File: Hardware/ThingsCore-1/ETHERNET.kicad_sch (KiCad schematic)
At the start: 1 part, among them U6 LAN8742A

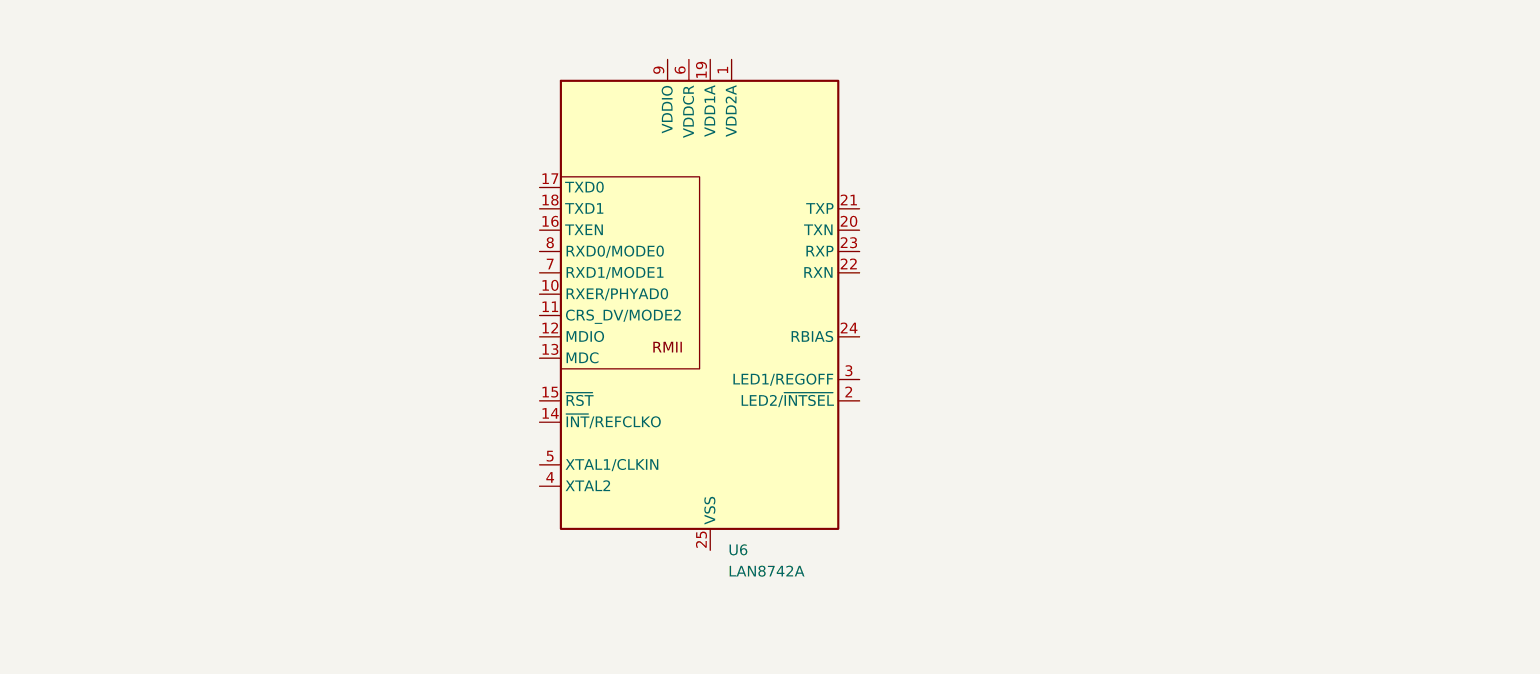
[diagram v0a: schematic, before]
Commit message: ddr3 fanout done
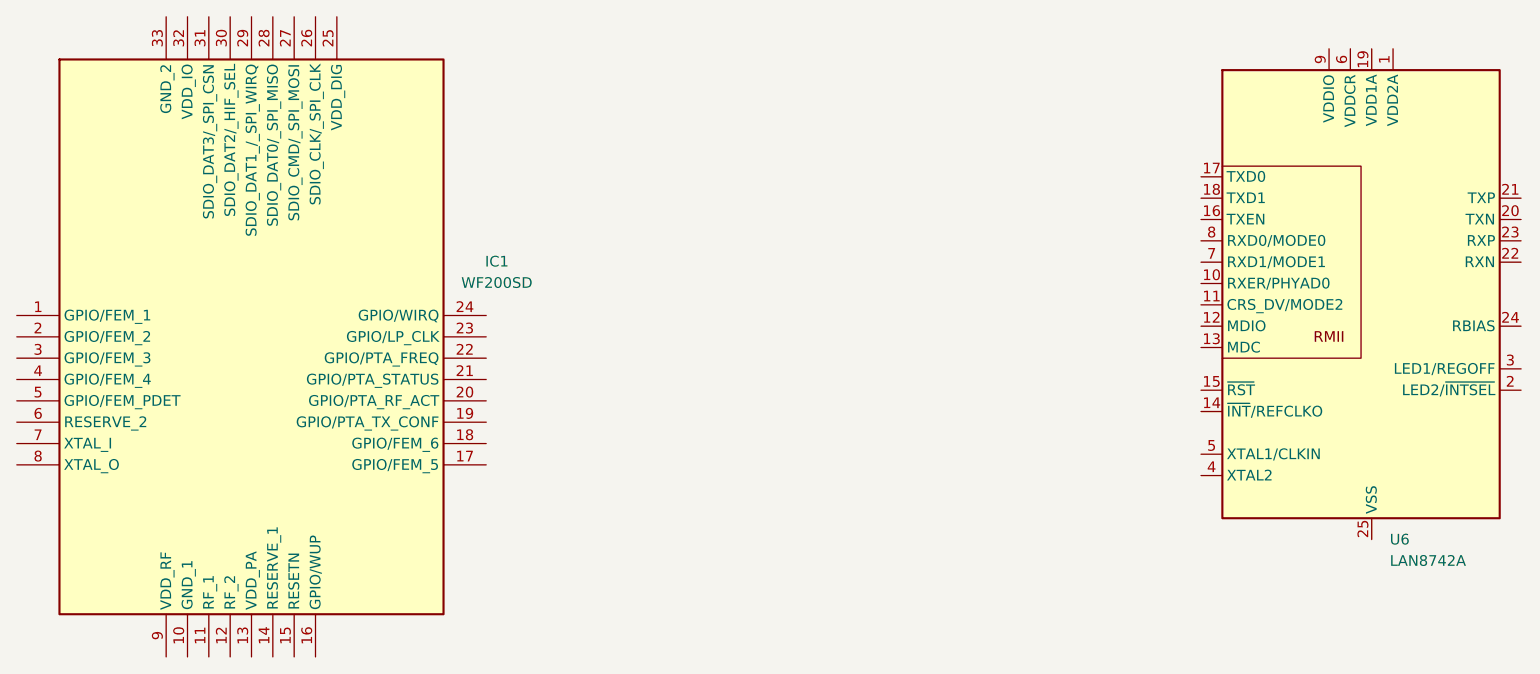
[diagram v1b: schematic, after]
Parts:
- added IC1: WF200SD, QFN40P400X400X90-33N-D, symbol ThingsCore-1:WF200SD
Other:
- moved on the sheet: U6
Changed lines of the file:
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@@
 	(symbol
 		(lib_id "Interface_Ethernet:LAN8742A")
-		(at 151.13 92.71 0)
+		(at 229.87 91.44 0)
 		(unit 1)
 		(exclude_from_sim no)
@@
 		(fields_autoplaced yes)
 		(property "Reference" "U6"
-			(at 153.2733 120.65 0)
+			(at 232.0133 119.38 0)
 			(effects
 				(font
@@
 		)
 		(property "Value" "LAN8742A"
-			(at 153.2733 123.19 0)
+			(at 232.0133 121.92 0)
 			(effects
 				(font
@@
 		)
 		(property "Footprint" "Package_DFN_QFN:VQFN-24-1EP_4x4mm_P0.5mm_EP2.45x2.45mm"
-			(at 152.4 119.38 0)
+			(at 231.14 118.11 0)
 			(effects
 				(font
@@
 		)
 		(property "Datasheet" "http://ww1.microchip.com/downloads/en/DeviceDoc/8742a.pdf"
-			(at 151.13 132.08 0)
+			(at 229.87 130.81 0)
 			(effects
 				(font
@@
 		)
 		(property "Description" "LAN8720 Ethernet PHY with RMII interface, QFN-24"
-			(at 151.13 92.71 0)
+			(at 229.87 91.44 0)
 			(effects
 				(font
@@
 					(unit 1)
 				)
+			)
+		)
+	)
+	(symbol
+		(lib_id "ThingsCore-1:WF200SD")
+		(at 68.58 92.71 0)
+		(unit 1)
+		(exclude_from_sim no)
+		(in_bom yes)
+		(on_board yes)
+		(dnp no)
+		(fields_autoplaced yes)
+		(property "Reference" "IC1"
+			(at 125.73 86.2898 0)
+			(effects
+				(font
+					(size 1.27 1.27)
+				)
+			)
+		)
+		(property "Value" "WF200SD"
+			(at 125.73 88.8298 0)
+			(effects
+				(font
+					(size 1.27 1.27)
+				)
+			)
+		)
+		(property "Footprint" "QFN40P400X400X90-33N-D"
+			(at 120.65 159.69 0)
+			(effects
+				(font
+					(size 1.27 1.27)
+				)
+				(justify left top)
+				(hide yes)
+			)
+		)
+		(property "Datasheet" "https://www.silabs.com/documents/public/data-sheets/wf200-datasheet.pdf"
+			(at 120.65 259.69 0)
+			(effects
+				(font
+					(size 1.27 1.27)
+				)
+				(justify left top)
+				(hide yes)
+			)
+		)
+		(property "Description" "WF200 802.11bgn NCP, Secure link interface, 4x4 QFN32"
+			(at 68.58 92.71 0)
+			(effects
+				(font
+					(size 1.27 1.27)
+				)
+				(hide yes)
+			)
+		)
+		(property "Height" "0.9"
+			(at 120.65 459.69 0)
+			(effects
+				(font
+					(size 1.27 1.27)
+				)
+				(justify left top)
+				(hide yes)
+			)
+		)
+		(property "Mouser Part Number" "634-WF200SD"
+			(at 120.65 559.69 0)
+			(effects
+				(font
+					(size 1.27 1.27)
+				)
+				(justify left top)
+				(hide yes)
+			)
+		)
+		(property "Mouser Price/Stock" "https://www.mouser.co.uk/ProductDetail/Silicon-Labs/WF200SD?qs=vEM7xhTegWgRA5s9PPW5sw%3D%3D"
+			(at 120.65 659.69 0)
+			(effects
+				(font
+					(size 1.27 1.27)
+				)
+				(justify left top)
+				(hide yes)
+			)
+		)
+		(property "Manufacturer_Name" "Silicon Labs"
+			(at 120.65 759.69 0)
+			(effects
+				(font
+					(size 1.27 1.27)
+				)
+				(justify left top)
+				(hide yes)
+			)
+		)
+		(property "Manufacturer_Part_Number" "WF200SD"
+			(at 120.65 859.69 0)
+			(effects
+				(font
+					(size 1.27 1.27)
+				)
+				(justify left top)
+				(hide yes)
+			)
+		)
+		(pin "13"
+		)
+		(pin "14"
+		)
+		(pin "5"
+		)
+		(pin "31"
+		)
+		(pin "7"
+		)
+		(pin "15"
+		)
+		(pin "4"
+		)
+		(pin "22"
+		)
+		(pin "17"
+		)
+		(pin "27"
+		)
+		(pin "11"
+		)
+		(pin "8"
+		)
+		(pin "6"
+		)
+		(pin "33"
+		)
+		(pin "21"
+		)
+		(pin "25"
+		)
+		(pin "3"
+		)
+		(pin "23"
+		)
+		(pin "20"
+		)
+		(pin "30"
+		)
+		(pin "19"
+		)
+		(pin "2"
+		)
+		(pin "26"
+		)
+		(pin "12"
+		)
+		(pin "9"
+		)
+		(pin "18"
+		)
+		(pin "10"
+		)
+		(pin "32"
+		)
+		(pin "1"
+		)
+		(pin "28"
+		)
+		(pin "16"
+		)
+		(pin "24"
+		)
+		(pin "29"
+		)
+		(instances
+			(project ""
+				(path "/0e14d4aa-2dd0-4b28-ae35-43afd1798b30/992f1809-ba75-41aa-9652-2a2392b25d6d"
+					(reference "IC1")
+					(unit 1)
+				)

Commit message: layout transciever components, pin selection and last components
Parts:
- added C101, C83, C98, C99: 100n, Capacitor_SMD:C_0402_1005Metric, symbol Device:C
- added C81: ~, Capacitor_SMD:C_0402_1005Metric, symbol Device:C
- added C82: 2.2u, Capacitor_SMD:C_0402_1005Metric, symbol Device:C
- added C84, C85, C87, C92, C97: 10u, Capacitor_SMD:C_0402_1005Metric, symbol Device:C
- added C86: 10n, Capacitor_SMD:C_0402_1005Metric, symbol Device:C
- added C88, C91: 33n, Capacitor_SMD:C_0402_1005Metric, symbol Device:C
- added C89, C90: 12p, Capacitor_SMD:C_0402_1005Metric, symbol Device:C
- added C93, C94: 15p, Capacitor_SMD:C_0402_1005Metric, symbol Device:C
- added C95: 1u, Capacitor_SMD:C_0402_1005Metric, symbol Device:C
- added C96: 470p, Capacitor_SMD:C_0402_1005Metric, symbol Device:C
- added FB1: 600Ω@100MHz, Inductor_SMD:L_0805_2012Metric, symbol Device:FerriteBead_Small
- added J1: Conn_Coaxial, Connector_Coaxial:U.FL_Molex_MCRF_73412-0110_Vertical, symbol Connector:Conn_Coaxial
- added L4: ~, Inductor_SMD:L_0402_1005Metric, symbol Device:L
- added R37: 50R, Resistor_SMD:R_0402_1005Metric, symbol Device:R
- added R38, R42: 0R, Resistor_SMD:R_0402_1005Metric, symbol Device:R
- added R39: 12.1k, Resistor_SMD:R_0402_1005Metric, symbol Device:R
- added R40, R41: 10K, Resistor_SMD:R_0402_1005Metric, symbol Device:R
- added R43, R44, R45, R46: 49R9, Resistor_SMD:R_0402_1005Metric, symbol Device:R
- added R47, R48, R49, R50, R51, R52, R55, R56, R57, R58, R59: 33R, Resistor_SMD:R_0402_1005Metric, symbol Device:R
- added R53, R54: 10k, Resistor_SMD:R_0402_1005Metric, symbol Device:R
- added RN4: 22, ThingsCore-1:RESCAXS50P400X160X55-16N, symbol Device:R_Pack08_Split
- added Y3: C3SB38.400F09E12, Crystal:Crystal_SMD_3225-4Pin_3.2x2.5mm, symbol Device:Crystal_GND24
- added Y4: X322525MOB4SI, Crystal:Crystal_SMD_3225-4Pin_3.2x2.5mm, symbol Device:Crystal_GND24
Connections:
- net 3V3_ETH_PHY: now reaches U6.1 (VDD2A)
- net 3V3_ETH_PHY: now also U6.19 (VDD1A), C97.2, C98.2, C99.2, FB1.2, R43.1, R44.1, R45.1, R46.1
- net RXER: now reaches U6.10 (RXER/PHYAD0)
- net RXER: now also R53.1
- net CRS_DV: now reaches U6.11 (CRS_DV/MODE2)
- net CRS_DV: now also R59.1
- net MDIO: now reaches U6.12 (MDIO)
- net MDIO: now also R55.1, R57.1
- net MDC: now reaches U6.13 (MDC)
- net MDC: now also R56.1, R58.1
- net REFCLKO: now reaches U6.14 (~{INT}/REFCLKO)
- net REFCLKO: now also R47.1
- net ETH_RST: now reaches U6.15 (~{RST})
- net ETH_RST: now also R54.1
- net TXEN: now reaches U6.16 (TXEN)
- net TXEN: now also R50.1
- net TXD0: now reaches U6.17 (TXD0)
- net TXD0: now also R48.1
- net TXD1: now reaches U6.18 (TXD1)
- net TXD1: now also R49.1
- net LED2: now reaches U6.2 (LED2/~{INTSEL})
- net LED2: now also R41.2, R42.1
- net TXN: now reaches U6.20 (TXN)
- net TXN: now also R45.2
- net TXP: now reaches U6.21 (TXP)
- net TXP: now also R46.2
- net RXN: now reaches U6.22 (RXN)
- net RXN: now also R43.2
- net RXP: now reaches U6.23 (RXP)
- net RXP: now also R44.2
- net RBIAS: now reaches U6.24 (RBIAS)
- net RBIAS: now also R39.2
- net GND: now reaches U6.25 (VSS)
- net GND: now also IC1.10 (GND_1), IC1.14 (RESERVE_1), IC1.23 (GPIO/LP_CLK), IC1.33 (GND_2), C101.1, C81.2, C82.2, C83.1, C84.1, C85.1, C86.1, C87.1, C88.1, C89.1, C90.1, C91.1, C92.1, C93.1, C94.1, C95.1, C96.1, C97.1, C98.1, C99.1, J1.2 (Ext), R37.1, R39.1, R40.1, R41.1, R53.2, R54.2, Y3.2, Y3.4, Y4.2, Y4.4
- net LED1: now reaches U6.3 (LED1/REGOFF)
- net LED1: now also R40.2
- net ETH_REF_OUT: now reaches U6.4 (XTAL2)
- net ETH_REF_OUT: now also C94.2, Y4.3
- net ETH_REF_IN: now reaches U6.5 (XTAL1/CLKIN)
- net ETH_REF_IN: now also C93.2, Y4.1
- net VDDCR: now reaches U6.6 (VDDCR)
- net VDDCR: now also C95.2, C96.2
- net RXD1: now reaches U6.7 (RXD1/MODE1)
- net RXD1: now also R52.1
- net RXD0: now reaches U6.8 (RXD0/MODE0)
- net RXD0: now also R51.1
- net 3V3_VDD: now reaches U6.9 (VDDIO)
- net 3V3_VDD: now also IC1.13 (VDD_PA), IC1.25 (VDD_DIG), IC1.32 (VDD_IO), IC1.9 (VDD_RF), C101.2, C83.2, C84.2, C85.2, C86.2, C87.2, C88.2, C89.2, C90.2, C91.2, C92.2, FB1.1, R57.2, R58.2
- net RF1: now reaches IC1.11 (RF_1)
- net RF1: now also C82.1, L4.1
- net RF2: now reaches IC1.12 (RF_2)
- net RF2: now also R37.2
- net TRX_~{RST}: now reaches IC1.15 (RESETN)
- net TRX_~{RST}: now also R38.2
- net TRX_WUP: now reaches IC1.16 (GPIO/WUP)
- net TRX_IRQ: now reaches IC1.24 (GPIO/WIRQ)
- net TRX_CLK: now reaches IC1.26 (SDIO_CLK/_SPI_CLK)
- net TRX_CLK: now also RN4.1 (R1.1)
- net TRX_CMD: now reaches IC1.27 (SDIO_CMD/_SPI_MOSI)
- net TRX_CMD: now also RN4.2 (R2.1)
- net TRX_D0: now reaches IC1.28 (SDIO_DAT0/_SPI_MISO)
- net TRX_D0: now also RN4.3 (R3.1)
- net TRX_D1: now reaches IC1.29 (SDIO_DAT1_/_SPI_WIRQ)
- net TRX_D1: now also RN4.4 (R4.1)
- net TRX_D2: now reaches IC1.30 (SDIO_DAT2/_HIF_SEL)
- net TRX_D2: now also RN4.5 (R5.1)
- net TRX_D3: now reaches IC1.31 (SDIO_DAT3/_SPI_CSN)
- net TRX_D3: now also RN4.6 (R6.1)
- net at IC1.7 (XTAL_I): now also Y3.3
- net at IC1.8 (XTAL_O): now also Y3.1
- new net: C81.1, J1.1 (In), L4.2
- new net ETH_CRS_DV: R59.2
- new net ETH_MDC: R56.2
- new net ETH_MDIO: R55.2
- new net ETH_REF_CLK: R47.2
- new net ETH_RX_D0: R51.2, R52.2
- new net ETH_TX_D0: R48.2
- new net ETH_TX_D1: R49.2
- new net ETH_TX_EN: R50.2
- new net ETH_~{INT}: R42.2
- new net MMC1_CLK: RN4.16 (R1.2)
- new net MMC1_CMD: RN4.15 (R2.2)
- new net MMC1_D0: RN4.14 (R3.2)
- new net MMC1_D1: RN4.13 (R4.2)
- new net MMC1_D2: RN4.12 (R5.2)
- new net MMC1_D3: RN4.11 (R6.2)
- new net NRST: R38.1
- no-connect marks 0 -> 12
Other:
- note added: "18.6+j9.6 Ω @2442MHz"
- note added: "ETH PHY"
- note added: "UG382"
- note added: "WF200 Datasheet: Crystal requirements P. 16"
- note added: "WIFI TRX"
- moved on the sheet: IC1, U6

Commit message: pin assignment, rst,led, button pins left and checks
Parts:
- removed RN4: 22, ThingsCore-1:RESCAXS50P400X160X55-16N, symbol Device:R_Pack08_Split
- added R25, R27, R60, R61, R62, R63: 33R, Resistor_SMD:R_0402_1005Metric, symbol Device:R
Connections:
- net NRST is gone; now on net TRX_~{RST}: R38.1
- net ETH_RX_D0: no longer R52.2
- net MMC1_CLK: now also R25.1
- net MMC1_CMD: now also R27.1
- net MMC1_D0: now also R60.1
- net MMC1_D1: now also R61.1
- net MMC1_D2: now also R62.1
- net MMC1_D3: now also R63.1
- net TRX_CLK: now also R25.2
- net TRX_CMD: now also R27.2
- net TRX_D0: now also R60.2
- net TRX_D1: now also R61.2
- net TRX_D2: now also R62.2
- net TRX_D3: now also R63.2
- net TRX_~{RST}: no longer IC1.15 (RESETN), R38.2
- new net ETH_RX_D1: R52.2
- new net TRX_RESETN: IC1.15 (RESETN), R38.2
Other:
- moved on the sheet: R57, R58

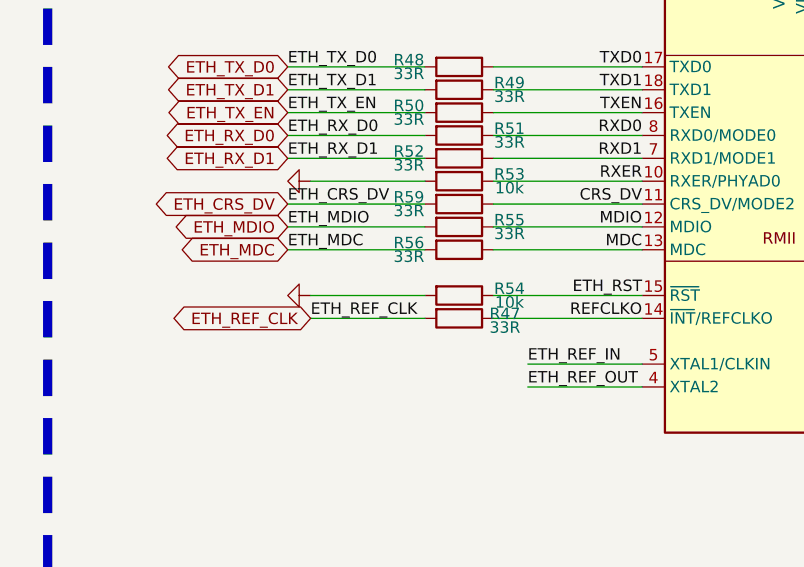
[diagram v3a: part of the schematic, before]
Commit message: checks left and feedback resistors for switchers
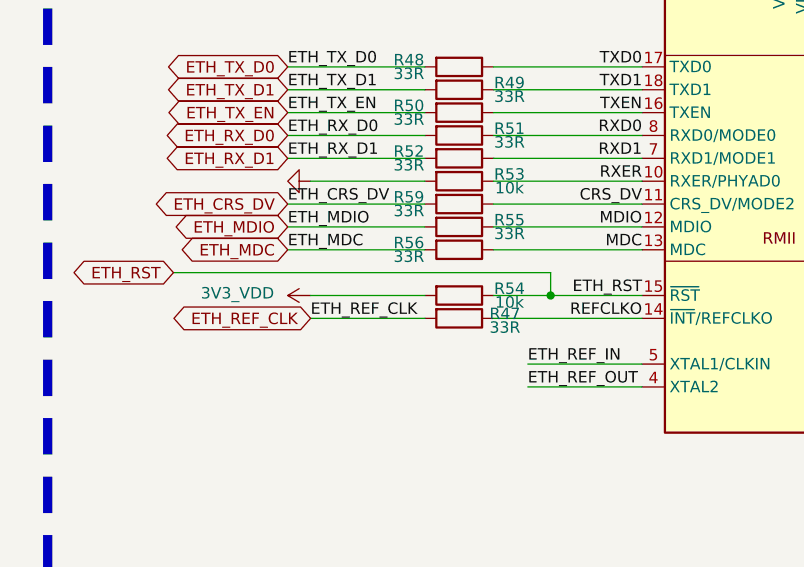
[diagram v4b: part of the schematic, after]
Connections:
- net 3V3_VDD: now also R54.2
- net GND: no longer R54.2
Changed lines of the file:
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@@
 	)
 	(junction
+		(at 78.74 142.24)
+		(diameter 0)
+		(color 0 0 0 0)
+	)
+	(junction
 		(at 276.86 102.87)
 		(diameter 0)
@@
 	(wire
 		(pts
+			(xy 36.83 139.7) (xy 78.74 139.7)
+		)
+		(stroke
+			(width 0)
+			(type default)
+		)
+	)
+	(wire
+		(pts
 			(xy 73.66 184.15) (xy 73.66 186.69)
 		)
@@
 	(wire
 		(pts
-			(xy 72.39 142.24) (xy 88.9 142.24)
+			(xy 72.39 142.24) (xy 78.74 142.24)
 		)
 		(stroke
@@
 	(wire
 		(pts
+			(xy 78.74 139.7) (xy 78.74 142.24)
+		)
+		(stroke
+			(width 0)
+			(type default)
+		)
+	)
+	(wire
+		(pts
 			(xy 248.92 149.86) (xy 260.35 149.86)
 		)
@@
 	(wire
 		(pts
+			(xy 78.74 142.24) (xy 88.9 142.24)
+		)
+		(stroke
+			(width 0)
+			(type default)
+		)
+	)
+	(wire
+		(pts
 			(xy 276.86 102.87) (xy 276.86 104.14)
 		)
@@
 		)
 	)
+	(global_label "ETH_RST"
+		(shape bidirectional)
+		(at 36.83 139.7 180)
+		(fields_autoplaced yes)
+		(effects
+			(font
+				(size 1.27 1.27)
+			)
+			(justify right)
+		)
+		(property "Intersheetrefs" "${INTERSHEET_REFS}"
+			(at 24.8717 139.7 0)
+			(effects
+				(font
+					(size 1.27 1.27)
+				)
+				(justify right)
+				(hide yes)
+			)
+		)
+	)
 	(global_label "LED1"
 		(shape bidirectional)
@@
 	)
 	(symbol
+		(lib_id "power:+1V0")
+		(at 52.07 142.24 90)
+		(mirror x)
+		(unit 1)
+		(exclude_from_sim no)
+		(in_bom yes)
+		(on_board yes)
+		(dnp no)
+		(property "Reference" "#PWR0127"
+			(at 55.88 142.24 0)
+			(effects
+				(font
+					(size 1.27 1.27)
+				)
+				(hide yes)
+			)
+		)
+		(property "Value" "3V3_VDD"
+			(at 43.942 141.986 90)
+			(effects
+				(font
+					(size 1.27 1.27)
+				)
+			)
+		)
+		(property "Footprint" ""
+			(at 52.07 142.24 0)
+			(effects
+				(font
+					(size 1.27 1.27)
+				)
+				(hide yes)
+			)
+		)
+		(property "Datasheet" ""
+			(at 52.07 142.24 0)
+			(effects
+				(font
+					(size 1.27 1.27)
+				)
+				(hide yes)
+			)
+		)
+		(property "Description" "Power symbol creates a global label with name \"+1V0\""
+			(at 52.07 142.24 0)
+			(effects
+				(font
+					(size 1.27 1.27)
+				)
+				(hide yes)
+			)
+		)
+		(pin "1"
+		)
+		(instances
+			(project "ThingsCore-1"
+				(path "/0e14d4aa-2dd0-4b28-ae35-43afd1798b30/992f1809-ba75-41aa-9652-2a2392b25d6d"
+					(reference "#PWR0127")
+					(unit 1)
+				)
+			)
+		)
+	)
+	(symbol
 		(lib_id "Device:R")
 		(at 264.16 149.86 90)
@@
 					(unit 1)
 				)
-			)
-		)
-	)
-	(symbol
-		(lib_id "power:GND")
-		(at 52.07 142.24 270)
-		(unit 1)
-		(exclude_from_sim no)
-		(in_bom yes)
-		(on_board yes)
-		(dnp no)
-		(fields_autoplaced yes)
-		(property "Reference" "#PWR0127"
-			(at 45.72 142.24 0)
-			(effects
-				(font
-					(size 1.27 1.27)
-				)
-				(hide yes)
-			)
-		)
-		(property "Value" "GND"
-			(at 46.99 142.24 0)
-			(effects
-				(font
-					(size 1.27 1.27)
-				)
-				(hide yes)
-			)
-		)
-		(property "Footprint" ""
-			(at 52.07 142.24 0)
-			(effects
-				(font
-					(size 1.27 1.27)
-				)
-				(hide yes)
-			)
-		)
-		(property "Datasheet" ""
-			(at 52.07 142.24 0)
-			(effects
-				(font
-					(size 1.27 1.27)
-				)
-				(hide yes)
-			)
-		)
-		(property "Description" "Power symbol creates a global label with name \"GND\" , ground"
-			(at 52.07 142.24 0)
-			(effects
-				(font
-					(size 1.27 1.27)
-				)
-				(hide yes)
-			)
-		)
-		(pin "1"
-		)
-		(instances
-			(project "ThingsCore-1"
-				(path "/0e14d4aa-2dd0-4b28-ae35-43afd1798b30/992f1809-ba75-41aa-9652-2a2392b25d6d"
-					(reference "#PWR0127")
-					(unit 1)
-				)
